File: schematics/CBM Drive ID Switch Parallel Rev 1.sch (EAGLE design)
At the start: 17 parts, among them IC1 MOS6522, IC2 ATMEGA48, IC3 2x20pin headers, IC4 74AHCT273, IC5 741G04, Y1 20MHz

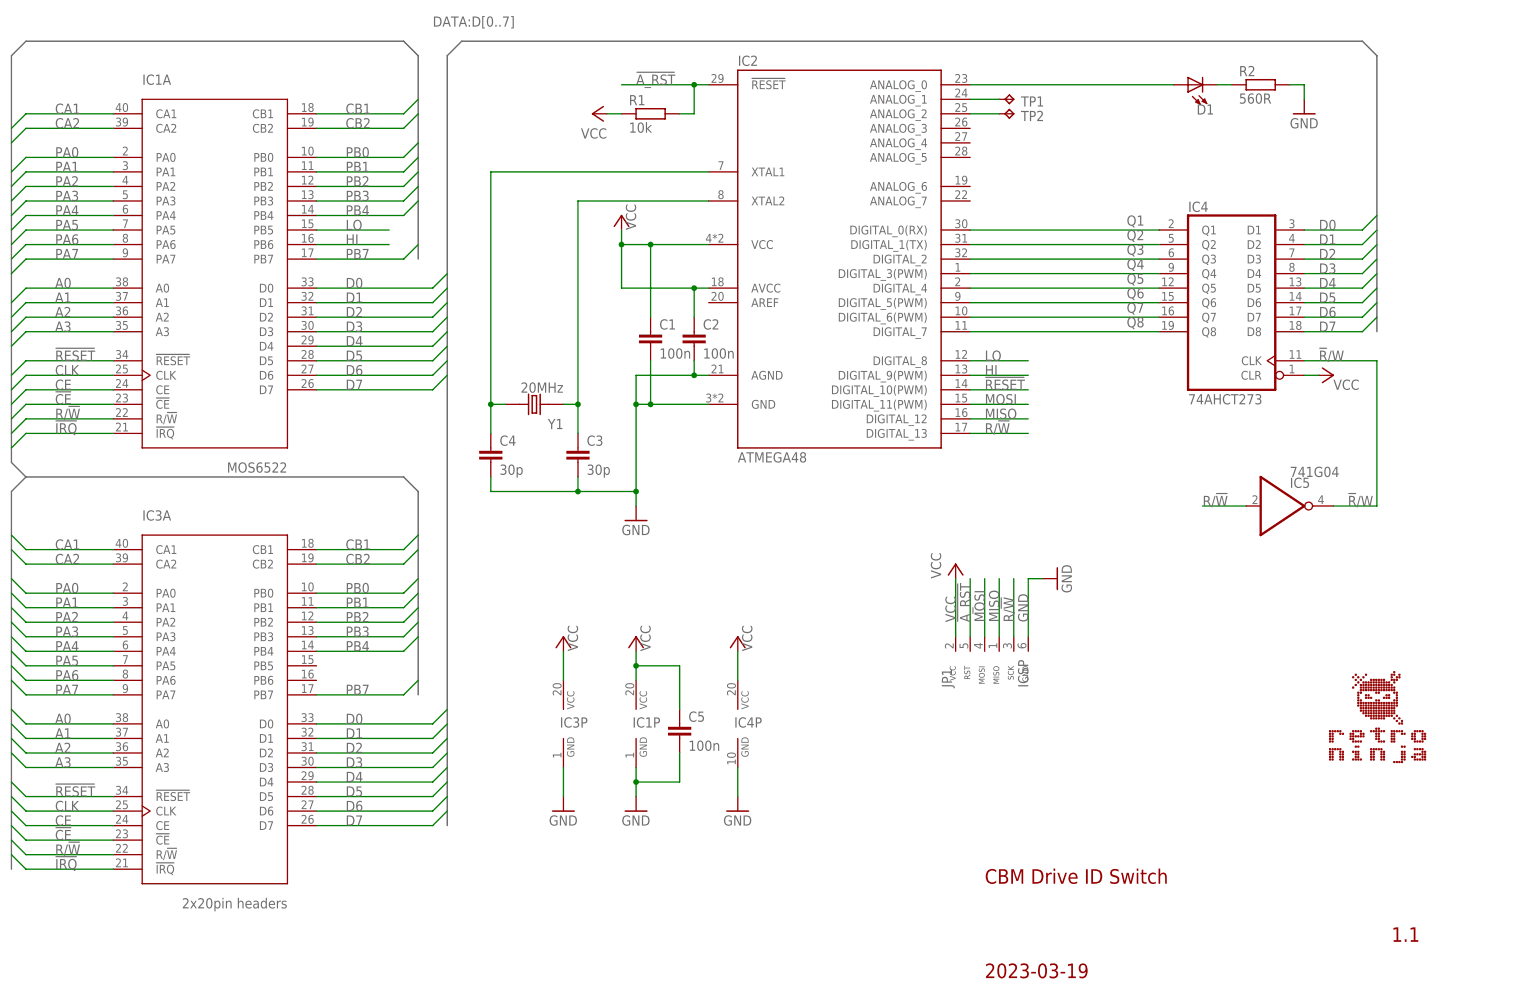
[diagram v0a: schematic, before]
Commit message: Added parallel adapter, added images, updated firmware (1.1) and README
Firmware 1.1 adds a short delay before resetting drive to prevent LOAD commnand from hanging some drives.
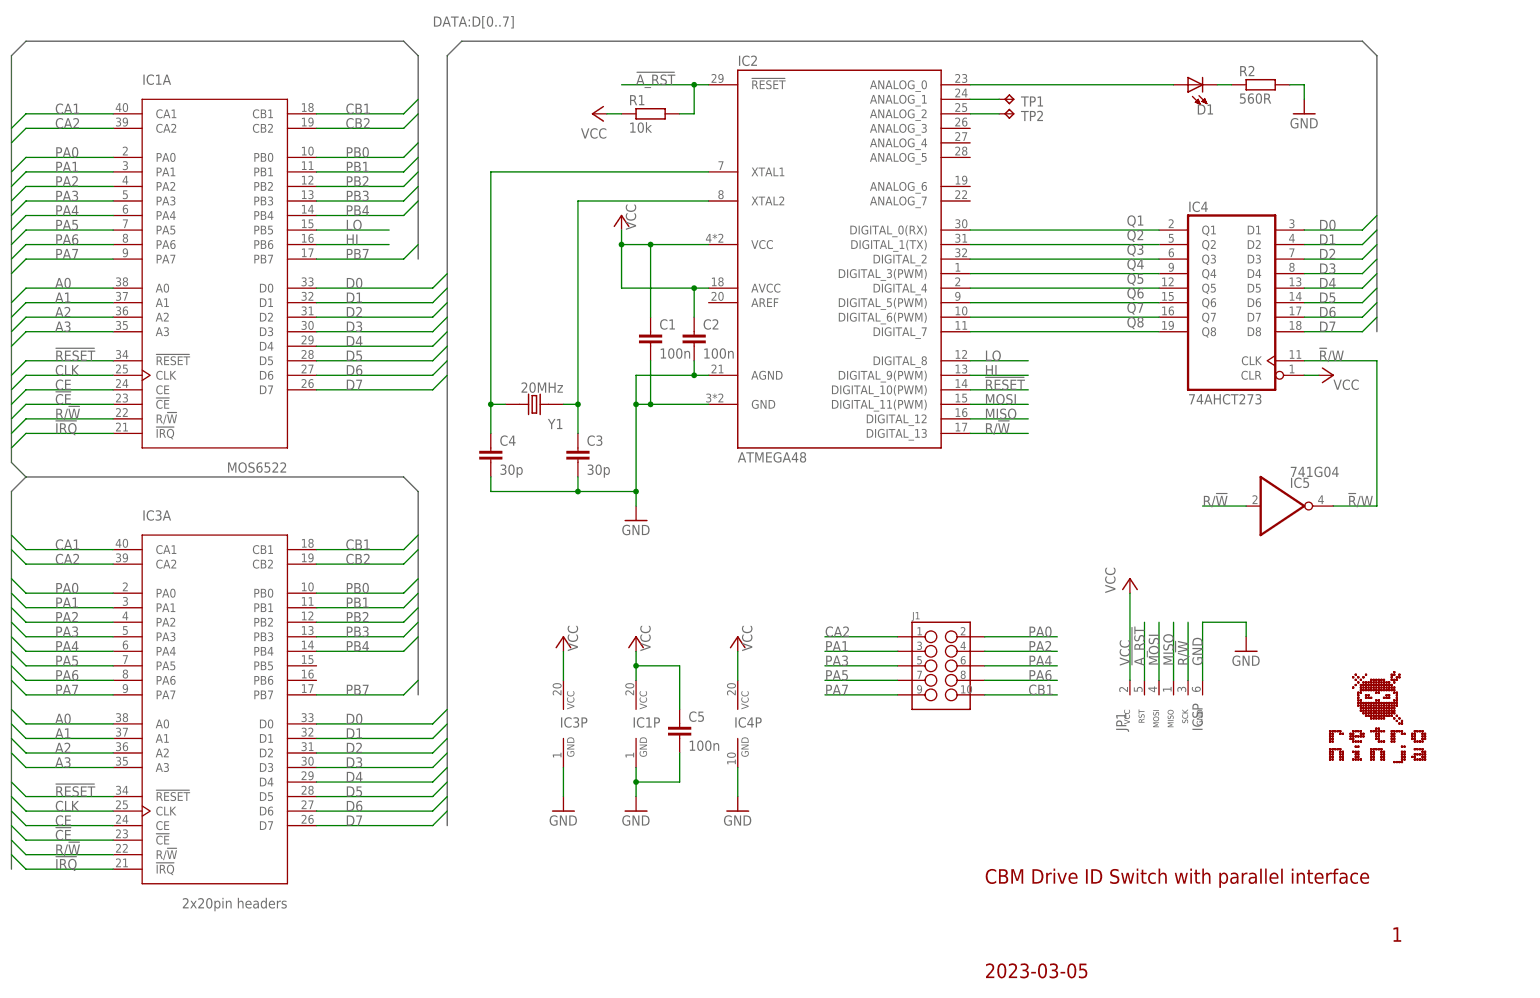
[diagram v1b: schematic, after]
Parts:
- added J1: (no value), Per (Fusion 360):HEADER_2X5-WALLED-90
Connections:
- net CA2: now also J1.1
- net CB1: now also J1.10
- net PA0: now also J1.2
- net PA1: now also J1.3
- net PA2: now also J1.4
- net PA3: now also J1.5
- net PA4: now also J1.6
- net PA5: now also J1.7
- net PA6: now also J1.8
- net PA7: now also J1.9
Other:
- note added: "1"
- note added: "2023-03-05"
- note added: "CBM Drive ID Switch with parallel interface"
- note removed: "1.1"
- note removed: "2023-03-19"
- note removed: "CBM Drive ID Switch"
- moved on the sheet: JP1
